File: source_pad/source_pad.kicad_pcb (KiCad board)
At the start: 2 copper layers, 61.9 x 61.9 mm, 24 parts, among them SW1 SW_PUSH, SW2 SW_PUSH, SW3 SW_PUSH, SW4 SW_PUSH, SW5 SW_PUSH, SW6 SW_PUSH, SW7 SW_PUSH, SW8 SW_PUSH, SW9 SW_PUSH, U1 ProMicro-kbd

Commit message: Updated clearances
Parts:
- D1, D2, D3, D4, D5, D6, D7, D8, D9: moved to B.Cu
- U1: footprint kbd:ProMicro_v3.5 -> kbd:ProMicro_v3.5_fix
- moved U1 4.90 mm to (119.0, 103.1)
- moved REF** 3.54 mm to (148.0, 90.0)
- moved REF** 3.54 mm to (90.0, 90.0)
- moved REF** 3.20 mm to (90.0, 148.0)
- moved REF** 3.20 mm to (148.0, 148.0)
- moved D1 1.50 mm to (100.0, 109.5)
- moved D2 1.50 mm to (100.0, 128.5)
- moved D3 1.50 mm to (100.0, 147.5)
- moved D4 1.50 mm to (119.0, 109.5)
- moved D5 1.50 mm to (119.0, 128.5)
- moved D6 1.50 mm to (119.0, 147.5)
- moved D7 1.50 mm to (138.0, 109.5)
- moved D8 1.50 mm to (138.0, 128.5)
- moved D9 1.50 mm to (138.0, 147.5)
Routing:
- net col0: track 86.4 -> 74.6 mm
- net row1: track 74.9 -> 83.7 mm
- net row0: track 44.8 -> 52.6 mm
- net row2: track 78.9 -> 85.0 mm
- net col2: track 53.8 -> 50.1 mm
- net Net-(D9-Pad2): track 17.0 -> 19.5 mm
- net Net-(D3-Pad2): track 16.9 -> 19.3 mm
- net Net-(D4-Pad2): track 17.4 -> 18.9 mm
- net Net-(D6-Pad2): track 17.6 -> 19.1 mm
- net col1: track 57.5 -> 56.7 mm
- net Net-(D2-Pad2): track 19.5 -> 18.9 mm
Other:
- board size 61.9 x 61.9 mm -> 68 x 68 mm
- board text added: "Source Pad Rev 0.2"
- board text removed: "Source Pad Rev 0.1"

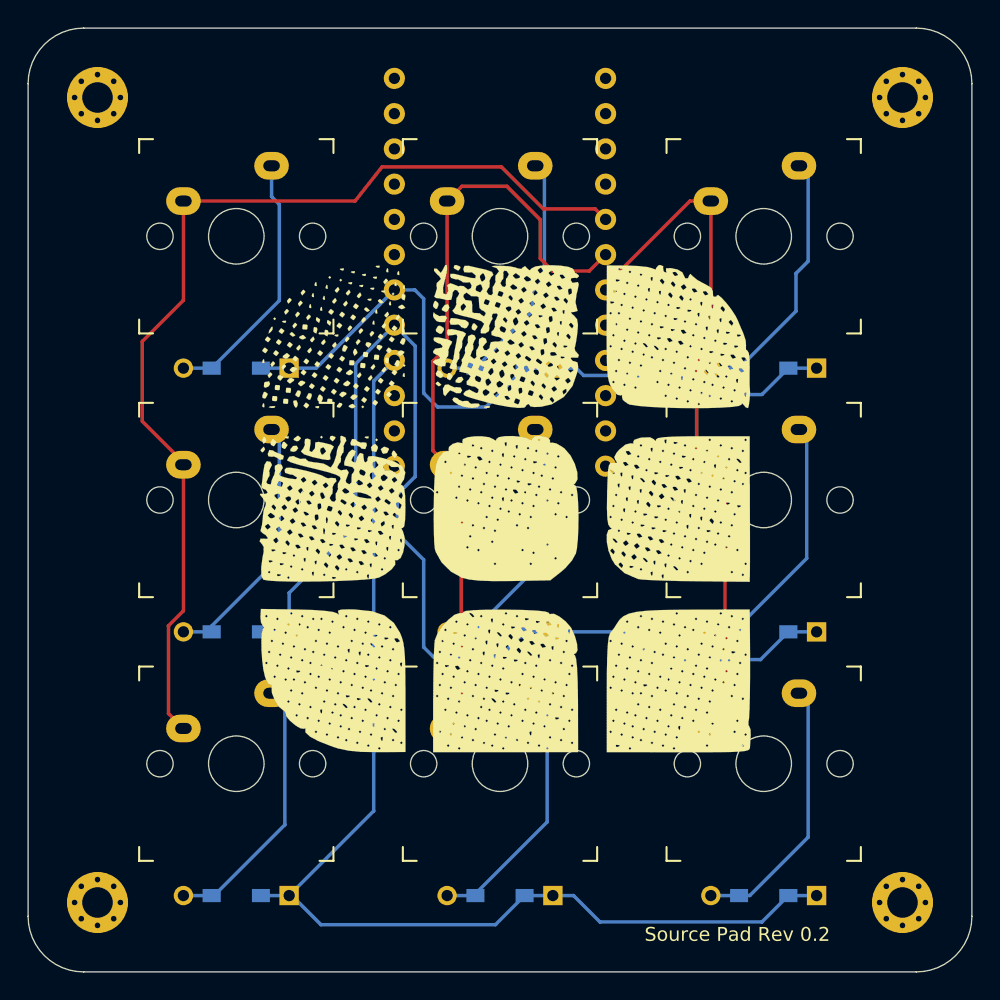
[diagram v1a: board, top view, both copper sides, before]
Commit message: Updated column traces
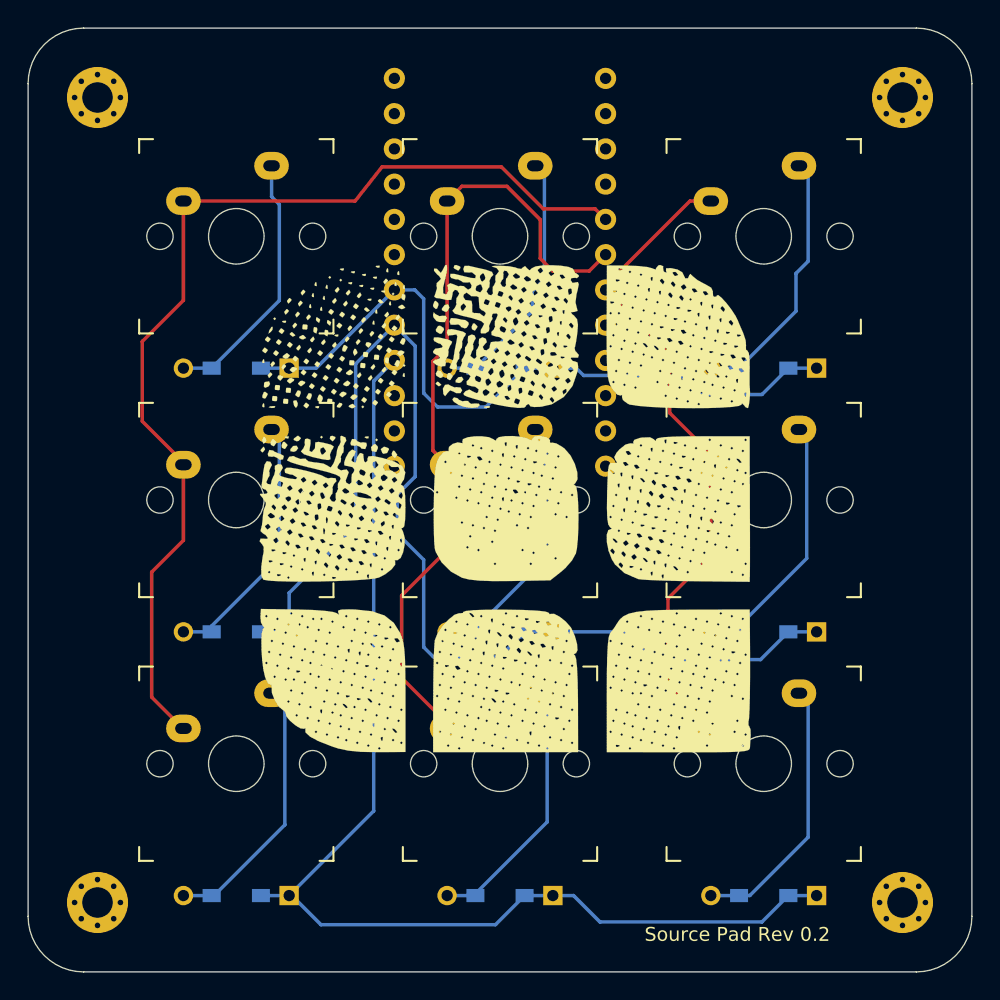
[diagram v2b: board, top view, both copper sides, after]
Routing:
- net col2: track 50.1 -> 47.7 mm
- net col1: track 56.7 -> 58.6 mm
- net col0: track 74.6 -> 75.6 mm
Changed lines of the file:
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@@
     (thickness 1.6)
     (drawings 9)
-    (tracks 141)
+    (tracks 146)
     (zones 0)
     (modules 24)
@@
   (segment (start 141.2 133.58) (end 140.54 132.92) (width 0.25) (layer B.Cu) (net 12))
   (segment (start 141.2 143.3) (end 141.2 133.58) (width 0.25) (layer B.Cu) (net 12))
-  (segment (start 95.112001 134.382001) (end 96.19 135.46) (width 0.25) (layer F.Cu) (net 13))
-  (segment (start 95.112001 128.063217) (end 95.112001 134.382001) (width 0.25) (layer F.Cu) (net 13))
-  (segment (start 96.19 126.985218) (end 95.112001 128.063217) (width 0.25) (layer F.Cu) (net 13))
-  (segment (start 96.19 116.46) (end 96.19 126.985218) (width 0.25) (layer F.Cu) (net 13))
   (segment (start 126.551599 98.724999) (end 126.6086 98.782) (width 0.25) (layer F.Cu) (net 13))
   (segment (start 96.19 97.46) (end 96.19 104.61) (width 0.25) (layer F.Cu) (net 13))
@@
   (segment (start 122.120001 98.020001) (end 125.846601 98.020001) (width 0.25) (layer F.Cu) (net 13))
   (segment (start 119.1 95) (end 122.120001 98.020001) (width 0.25) (layer F.Cu) (net 13))
+  (segment (start 96.19 135.46) (end 96.16 135.46) (width 0.25) (layer F.Cu) (net 13))
+  (segment (start 96.16 135.46) (end 93.9 133.2) (width 0.25) (layer F.Cu) (net 13))
+  (segment (start 93.9 133.2) (end 93.9 124.2) (width 0.25) (layer F.Cu) (net 13))
+  (segment (start 96.19 121.91) (end 96.19 116.46) (width 0.25) (layer F.Cu) (net 13))
+  (segment (start 93.9 124.2) (end 96.19 121.91) (width 0.25) (layer F.Cu) (net 13))
   (segment (start 114.166499 115.436499) (end 115.19 116.46) (width 0.25) (layer F.Cu) (net 14))
   (segment (start 114.166499 109.008719) (end 114.166499 115.436499) (width 0.25) (layer F.Cu) (net 14))
   (segment (start 115.19 107.985218) (end 114.166499 109.008719) (width 0.25) (layer F.Cu) (net 14))
   (segment (start 115.19 97.46) (end 115.19 107.985218) (width 0.25) (layer F.Cu) (net 14))
-  (segment (start 116.213501 134.436499) (end 115.19 135.46) (width 0.25) (layer F.Cu) (net 14))
-  (segment (start 116.213501 117.483501) (end 116.213501 134.436499) (width 0.25) (layer F.Cu) (net 14))
-  (segment (start 115.19 116.46) (end 116.213501 117.483501) (width 0.25) (layer F.Cu) (net 14))
   (segment (start 126.2306 101.7) (end 126.6086 101.322) (width 0.25) (layer F.Cu) (net 14))
   (segment (start 126.6086 101.322) (end 125.4306 102.5) (width 0.25) (layer F.Cu) (net 14))
@@
   (segment (start 119.5 96.4) (end 116.25 96.4) (width 0.25) (layer F.Cu) (net 14))
   (segment (start 116.25 96.4) (end 115.19 97.46) (width 0.25) (layer F.Cu) (net 14))
+  (segment (start 115.19 135.46) (end 115.19 135.09) (width 0.25) (layer F.Cu) (net 14))
+  (segment (start 111.910361 131.810361) (end 111.910361 125.889639) (width 0.25) (layer F.Cu) (net 14))
+  (segment (start 115.19 135.09) (end 111.910361 131.810361) (width 0.25) (layer F.Cu) (net 14))
+  (segment (start 115.19 122.61) (end 115.19 116.46) (width 0.25) (layer F.Cu) (net 14))
+  (segment (start 111.910361 125.889639) (end 115.19 122.61) (width 0.25) (layer F.Cu) (net 14))
   (segment (start 126.6086 103.5414) (end 126.6086 103.862) (width 0.25) (layer F.Cu) (net 15))
   (segment (start 132.69 97.46) (end 126.6086 103.5414) (width 0.25) (layer F.Cu) (net 15))
   (segment (start 134.19 97.46) (end 132.69 97.46) (width 0.25) (layer F.Cu) (net 15))
-  (segment (start 133.166499 115.436499) (end 134.19 116.46) (width 0.25) (layer F.Cu) (net 15))
-  (segment (start 133.166499 109.008719) (end 133.166499 115.436499) (width 0.25) (layer F.Cu) (net 15))
-  (segment (start 134.19 107.985218) (end 133.166499 109.008719) (width 0.25) (layer F.Cu) (net 15))
-  (segment (start 134.19 97.46) (end 134.19 107.985218) (width 0.25) (layer F.Cu) (net 15))
-  (segment (start 135.213501 134.436499) (end 134.19 135.46) (width 0.25) (layer F.Cu) (net 15))
-  (segment (start 135.213501 117.483501) (end 135.213501 134.436499) (width 0.25) (layer F.Cu) (net 15))
-  (segment (start 134.19 116.46) (end 135.213501 117.483501) (width 0.25) (layer F.Cu) (net 15))
+  (segment (start 134.19 116.46) (end 134.19 115.69) (width 0.25) (layer F.Cu) (net 15))
+  (segment (start 131.224999 108.478399) (end 126.6086 103.862) (width 0.25) (layer F.Cu) (net 15))
+  (segment (start 131.224999 112.724999) (end 131.224999 108.478399) (width 0.25) (layer F.Cu) (net 15))
+  (segment (start 134.19 115.69) (end 131.224999 112.724999) (width 0.25) (layer F.Cu) (net 15))
+  (segment (start 134.19 135.46) (end 134.19 135.39) (width 0.25) (layer F.Cu) (net 15))
+  (segment (start 134.19 135.39) (end 131.1 132.3) (width 0.25) (layer F.Cu) (net 15))
+  (segment (start 131.1 132.3) (end 131.1 126.1) (width 0.25) (layer F.Cu) (net 15))
+  (segment (start 134.19 123.01) (end 134.19 116.46) (width 0.25) (layer F.Cu) (net 15))
+  (segment (start 131.1 126.1) (end 134.19 123.01) (width 0.25) (layer F.Cu) (net 15))
 )

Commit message: Added makefile
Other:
- board text added: "JLCJLCJLCJLC"
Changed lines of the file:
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@@
   (general
     (thickness 1.6)
-    (drawings 9)
+    (drawings 10)
     (tracks 146)
     (zones 0)
@@
     (35 F.Paste user)
     (36 B.SilkS user)
-    (37 F.SilkS user hide)
+    (37 F.SilkS user)
     (38 B.Mask user)
     (39 F.Mask user)
@@
       (drillshape 0)
       (scaleselection 1)
-      (outputdirectory ""))
+      (outputdirectory "gerber/"))
   )
   (net 0 "")
@@
       (net 33 "Net-(U1-Pad24)"))
   )
+  (gr_text JLCJLCJLCJLC (at 98.5 150.8) (layer B.SilkS)
+    (effects (font (size 1 1) (thickness 0.15)) (justify mirror))
+  )
   (gr_line (start 85 149) (end 85 89) (layer Edge.Cuts) (width 0.05))

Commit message: fixed mx pads
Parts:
- SW1, SW2, SW3, SW4, SW5, SW6, SW7, SW8, SW9: footprint kbd:CherryMX_1u -> kbd:CherryMX_1u_fix
